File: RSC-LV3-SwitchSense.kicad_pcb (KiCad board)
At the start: 2 copper layers, 140 x 85 mm, 169 parts, among them J1 FTSH-105-01-L-DV-K-A, J10 Molex 43045-0400, J11 Molex 43045-0400, J12 Molex 43045-0400, J13 Molex 43045-0400, J14 Molex 43045-0400, J15 Molex 43045-0400, J16 Molex 43650-0200, J2 USB_C_Receptacle_USB2.0_16P, J3 Molex 43650-0500, J4 Molex 43650-0500, J5 Molex 43650-0200, J6 Molex 43045-0400, J7 Molex 43045-0400, J8 Molex 43045-0400, J9 Molex 43045-0400, Q1 AO3400A, Q10 AO3400A, Q2 AO3400A, Q3 AO3400A, Q4 AO3400A, Q5 AO3400A, Q6 AO3400A, Q7 AO3400A, Q8 AO3400A, Q9 AO3400A, U1 STM32G0B1CBTx, U2 TPS54302, U3 TLV74033PDBVR, U4 TJA1051T-3, U5 TJA1051T-3, Y1 Crystal_GND24, Y2 32.768 kHz 6pF

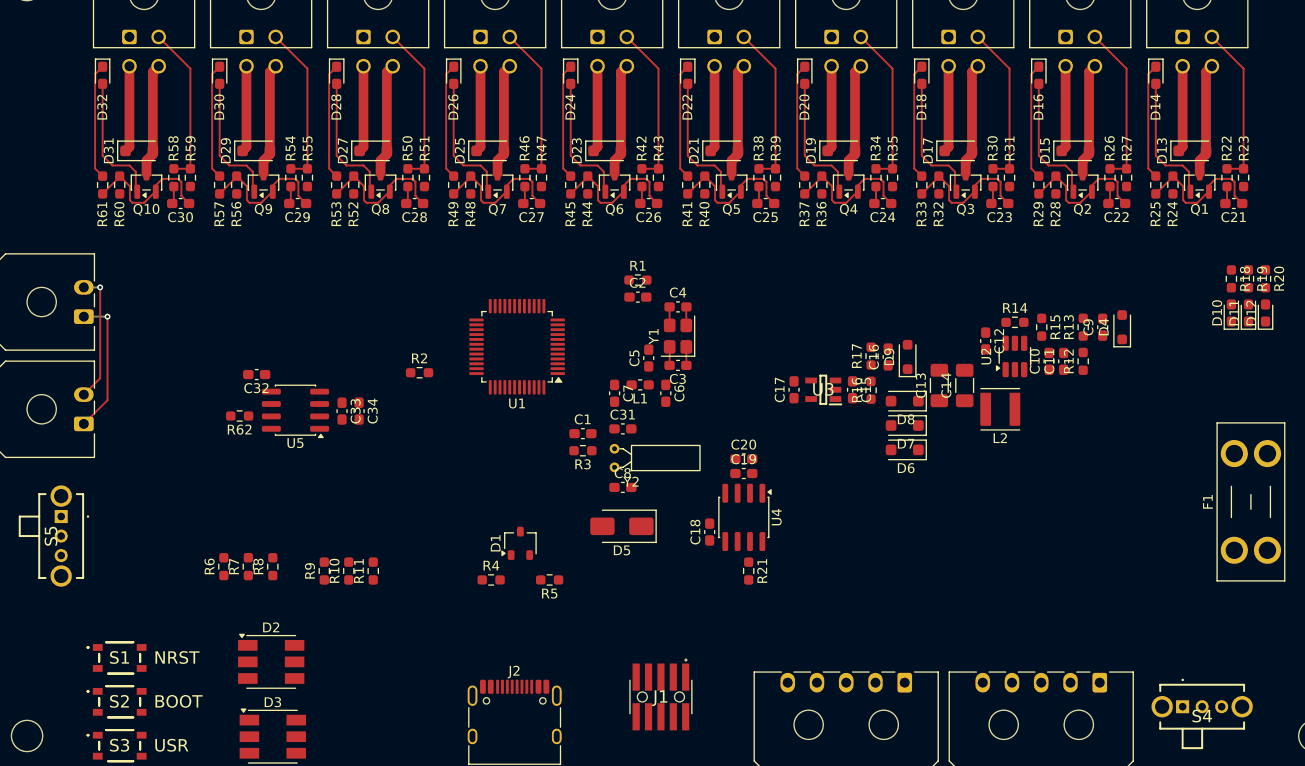
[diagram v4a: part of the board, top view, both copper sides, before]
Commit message: dual H/V compatible Molex footprints, corrected STM32 pinout
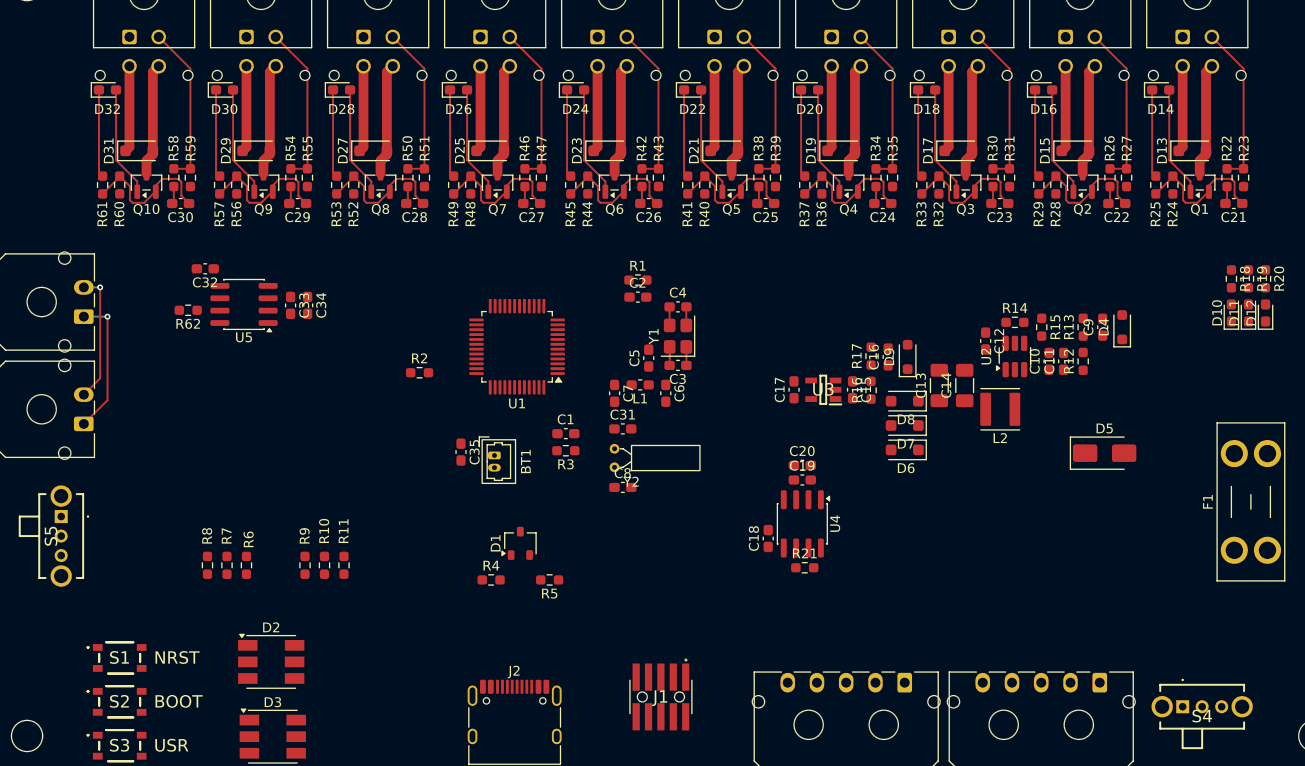
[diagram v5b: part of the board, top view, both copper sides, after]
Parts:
- added BT1: Molex 53047-0210, Connector_Molex:Molex_PicoBlade_53047-0210_1x02_P1.25mm_Vertical, F.Cu at (121.9, 102.2)
- added C35: 1u, Capacitor_SMD:C_0603_1608Metric_Pad1.08x0.95mm_HandSolder, F.Cu at (118.5, 101.9)
- J10, J11, J12, J13, J14, J15, J6, J7, J8, J9: footprint Connector_Molex:Molex_Micro-Fit_3.0_43045-0400_2x02_P3.00mm_Horizontal -> Project_Library:Molex_Micro-Fit_3.0_43045-0400_2x02_P3.00mm_Horizontal_VerticalCompatible
- J16, J5: footprint Connector_Molex:Molex_Micro-Fit_3.0_43650-0200_1x02_P3.00mm_Horizontal -> Project_Library:Molex_Micro-Fit_3.0_43650-0200_1x02_P3.00mm_Horizontal_VerticalCompatible
- J3, J4: footprint Connector_Molex:Molex_Micro-Fit_3.0_43650-0500_1x05_P3.00mm_Horizontal -> Project_Library:Molex_Micro-Fit_3.0_43650-0500_1x05_P3.00mm_Horizontal_VerticalCompatible
- moved D5 50.1 mm to (184.5, 102.0), turned to 0 degrees
- moved U5 12.1 mm to (96.2, 86.8)
- moved C32 12.1 mm to (92.3, 83.1)
- moved C33 12.1 mm to (101.0, 86.8)
- moved C34 12.1 mm to (102.8, 86.8)
- moved R62 12.1 mm to (90.5, 87.3)
- moved R8 6.70 mm to (92.5, 113.5), turned to -90 degrees
- moved C18 6.04 mm to (150.0, 110.8)
- moved C19 6.04 mm to (153.5, 104.8)
- moved C20 6.04 mm to (153.5, 103.2)
- moved U4 6.04 mm to (153.5, 109.2)
- moved R21 5.76 mm to (153.8, 113.8), turned to 0 degrees
- moved R11 3.06 mm to (106.5, 113.5)
- moved R10 2.56 mm to (104.5, 113.5)
- moved R6 2.32 mm to (96.5, 113.5), turned to -90 degrees
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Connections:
- J1 pad 2: BOOT0 -> SWD_IO
- J1 pad 4: SWD_CLK -> BOOT0
- U1 pad 25: unconnected-(U1-PB13-Pad25) -> FDCAN2_TX
- U1 pad 31: unconnected-(U1-PC7-Pad31) -> OUT_2
- U1 pad 35: SWD_CLK -> SWD_IO
- U1 pad 38: FDCAN1_TX -> FDCAN1_RX
- U1 pad 39: FDCAN1_RX -> FDCAN1_TX
- U1 pad 4: unconnected-(U1-VBAT-Pad4) -> Net-(BT1-+)
- U1 pad 44: OUT_2 -> FDCAN2_RX
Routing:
- net Net-(D32-K): track 11.9 -> 8.92 mm
- net Net-(D30-K): track 11.9 -> 8.92 mm
- net Net-(D26-K): track 11.9 -> 8.92 mm
- net Net-(D22-K): track 11.9 -> 8.92 mm
- net Net-(D20-K): track 11.9 -> 8.92 mm
- net Net-(D16-K): track 11.9 -> 8.92 mm
- net Net-(D28-K): track 11.9 -> 8.92 mm
- net Net-(D24-K): track 11.9 -> 8.92 mm
- net Net-(D18-K): track 11.9 -> 8.92 mm
- net Net-(D14-K): track 11.9 -> 8.92 mm
- net OUT_7: track 13.6 -> 11.2 mm
- net OUT_6: track 13.6 -> 11.2 mm
- net OUT_5: track 13.6 -> 11.2 mm
- net OUT_4: track 13.6 -> 11.2 mm
- net OUT_3: track 13.6 -> 11.2 mm
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
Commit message: initial routing
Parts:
- moved R1 54.2 mm to (91.0, 113.5), turned to 90 degrees
- moved C2 51.6 mm to (93.0, 113.5), turned to 90 degrees
- moved R21 35.3 mm to (189.0, 115.0)
- moved C1 34.0 mm to (98.0, 113.5), turned to 90 degrees
- moved R3 31.5 mm to (100.0, 113.5), turned to -90 degrees
- moved R2 27.2 mm to (95.5, 113.5), turned to -90 degrees
- moved BT1 23.0 mm to (144.8, 105.0)
- moved C35 19.9 mm to (138.0, 98.0)
- moved R62 14.2 mm to (90.2, 101.5), turned to -90 degrees
- moved R8 14.0 mm to (106.5, 113.5)
- moved R18 12.4 mm to (205.2, 93.8), turned to 90 degrees
- moved R20 10.2 mm to (197.8, 93.8), turned to 90 degrees
- moved R7 10.0 mm to (104.5, 113.5)
- moved R19 9.88 mm to (201.5, 93.8), turned to 90 degrees
- moved D10 7.97 mm to (205.2, 89.5), turned to -90 degrees
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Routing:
- net +5V_USB: track 0.00 -> 78.9 mm
- net PRIMARY_CAN-: track 0.00 -> 59.7 mm, vias 0 -> 2
- net +12V_IN: track 0.00 -> 59.7 mm
- net +5V_BUS: track 0.00 -> 57.8 mm, vias 0 -> 2
- net PRIMARY_CAN+: track 0.00 -> 57.4 mm, vias 0 -> 3
- net BTN_USR1: track 0.00 -> 30.3 mm
- net +3.3V: track 0.00 -> 29.8 mm
- net AUX_CAN+: track 13.4 -> 39.6 mm, vias 1 -> 3
- net AUX_CAN-: track 14.4 -> 38.8 mm
- net Net-(D3-RK): track 0.00 -> 23.4 mm
- net +5V: track 0.00 -> 23.0 mm
- net BOOT0: track 0.00 -> 22.7 mm
- net +5V_BUCK: track 0.00 -> 21.3 mm, vias 0 -> 2
- net Net-(D3-GK): track 0.00 -> 20.8 mm
- net Net-(S5-NO): track 0.00 -> 19.9 mm
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
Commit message: more non-autorouting adjustments
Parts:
- moved BT1 0.75 mm to (144.8, 105.8)
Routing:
- net USB-: track 14.3 -> 37.1 mm
- net USB+: track 14.3 -> 36.4 mm
- net GND: track 165.8 -> 167.5 mm, vias 0 -> 1
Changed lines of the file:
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@@
 	(footprint "Connector_Molex:Molex_PicoBlade_53047-0210_1x02_P1.25mm_Vertical"
 		(layer "F.Cu")
-		(at 144.75 105 -90)
+		(at 144.75 105.75 -90)
 		(descr "Molex PicoBlade Connector System, 53047-0210, 2 Pins per row (http://www.molex.com/pdm_docs/sd/530470610_sd.pdf)")
 		(tags "connector Molex PicoBlade vertical")
@@
 	)
 	(segment
+		(start 124.5 112.3)
+		(end 124.5 114)
+		(width 0.2)
+		(layer "F.Cu")
+		(net "GND")
+	)
+	(segment
 		(start 168.55 74.6375)
 		(end 168.55 76.065552)
@@
 		(net "GND")
 	)
+	(via
+		(at 124.5 114)
+		(size 0.6)
+		(drill 0.3)
+		(layers "F.Cu" "B.Cu")
+		(net "GND")
+	)
 	(segment
 		(start 81.375 73.2125)
@@
 	)
 	(segment
-		(start 137 99.166722)
-		(end 137 98.1375)
+		(start 143.583278 105.75)
+		(end 137 99.166722)
 		(width 0.2)
 		(layer "F.Cu")
@@
 	)
 	(segment
-		(start 142.833278 105)
-		(end 137 99.166722)
+		(start 137 98.1375)
+		(end 138 97.1375)
 		(width 0.2)
 		(layer "F.Cu")
@@
 	)
 	(segment
-		(start 144.75 105)
-		(end 142.833278 105)
+		(start 137 99.166722)
+		(end 137 98.1375)
 		(width 0.2)
 		(layer "F.Cu")
@@
 	)
 	(segment
-		(start 137 98.1375)
-		(end 138 97.1375)
+		(start 144.75 105.75)
+		(end 143.583278 105.75)
 		(width 0.2)
 		(layer "F.Cu")
@@
 	)
 	(segment
+		(start 125.15 113.649999)
+		(end 125.45 113.949999)
+		(width 0.2)
+		(layer "F.Cu")
+		(net "USB+")
+	)
+	(segment
+		(start 122.475 97.593198)
+		(end 122.475 106.906802)
+		(width 0.2)
+		(layer "F.Cu")
+		(net "USB+")
+	)
+	(segment
 		(start 124.75 124.867499)
 		(end 124.725 124.842499)
@@
 	)
 	(segment
+		(start 124.706249 96.725)
+		(end 123.343198 96.725)
+		(width 0.2)
+		(layer "F.Cu")
+		(net "USB+")
+	)
+	(segment
+		(start 122.475 106.906802)
+		(end 124.725 109.156802)
+		(width 0.2)
+		(layer "F.Cu")
+		(net "USB+")
+	)
+	(segment
 		(start 124.75 126.71241)
 		(end 124.75 125.955)
@@
 	)
 	(segment
+		(start 125.8375 96.75)
+		(end 124.731249 96.75)
+		(width 0.2)
+		(layer "F.Cu")
+		(net "USB+")
+	)
+	(segment
 		(start 124.48241 126.98)
 		(end 124.75 126.71241)
@@
 	)
 	(segment
+		(start 123.343198 96.725)
+		(end 122.475 97.593198)
+		(width 0.2)
+		(layer "F.Cu")
+		(net "USB+")
+	)
+	(segment
 		(start 124.01759 126.98)
 		(end 124.48241 126.98)
@@
 	)
 	(segment
+		(start 125.15 111.773398)
+		(end 125.15 113.649999)
+		(width 0.2)
+		(layer "F.Cu")
+		(net "USB+")
+	)
+	(segment
+		(start 124.725 109.156802)
+		(end 124.725 111.348398)
+		(width 0.2)
+		(layer "F.Cu")
+		(net "USB+")
+	)
+	(segment
+		(start 124.731249 96.75)
+		(end 124.706249 96.725)
+		(width 0.2)
+		(layer "F.Cu")
+		(net "USB+")
+	)
+	(segment
 		(start 124.725 116.175001)
 		(end 125.45 115.450001)
@@
 	)
 	(segment
+		(start 124.725 111.348398)
+		(end 125.15 111.773398)
+		(width 0.2)
+		(layer "F.Cu")
+		(net "USB+")
+	)
+	(segment
+		(start 125.45 113.949999)
+		(end 125.45 114.7)
+		(width 0.2)
+		(layer "F.Cu")
+		(net "USB+")
+	)
+	(segment
 		(start 123.55 115.450001)
 		(end 123.55 114.7)
@@
 	)
 	(segment
+		(start 122.025 97.406802)
+		(end 122.025 107.093198)
+		(width 0.2)
+		(layer "F.Cu")
+		(net "USB-")
+	)
+	(segment
 		(start 124.25 124.867499)
 		(end 124.275 124.842499)
@@
 	)
 	(segment
+		(start 124.275 109.343198)
+		(end 124.275 111.348398)
+		(width 0.2)
+		(layer "F.Cu")
+		(net "USB-")
+	)
+	(segment
 		(start 123.51759 124.93)
 		(end 123.25 125.19759)
@@
 	)
 	(segment
+		(start 124.275 111.348398)
+		(end 123.85 111.773398)
+		(width 0.2)
+		(layer "F.Cu")
+		(net "USB-")
+	)
+	(segment
+		(start 123.85 113.649999)
+		(end 123.55 113.949999)
+		(width 0.2)
+		(layer "F.Cu")
+		(net "USB-")
+	)
+	(segment
+		(start 123.55 113.949999)
+		(end 123.55 114.7)
+		(width 0.2)
+		(layer "F.Cu")
+		(net "USB-")
+	)
+	(segment
+		(start 125.8375 96.25)
+		(end 124.731249 96.25)
+		(width 0.2)
+		(layer "F.Cu")
+		(net "USB-")
+	)
+	(segment
+		(start 124.706249 96.275)
+		(end 123.156802 96.275)
+		(width 0.2)
+		(layer "F.Cu")
+		(net "USB-")
+	)
+	(segment
 		(start 124.275 116.175001)
 		(end 123.55 115.450001)
@@
 	)
 	(segment
+		(start 123.85 111.773398)
+		(end 123.85 113.649999)
+		(width 0.2)
+		(layer "F.Cu")
+		(net "USB-")
+	)
+	(segment
+		(start 123.156802 96.275)
+		(end 122.025 97.406802)
+		(width 0.2)
+		(layer "F.Cu")
+		(net "USB-")
+	)
+	(segment
+		(start 124.731249 96.25)
+		(end 124.706249 96.275)
+		(width 0.2)
+		(layer "F.Cu")
+		(net "USB-")
+	)
+	(segment
 		(start 123.25 125.19759)
 		(end 123.25 125.955)
 		(width 0.2)
 		(layer "F.Cu")
+		(net "USB-")
+	)
+	(segment
+		(start 122.025 107.093198)
+		(end 124.275 109.343198)
+		(width 0.2)
+		(layer "F.Cu")

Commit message: initial complete route
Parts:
- moved C32 1.75 mm to (94.0, 83.2), turned to 0 degrees
- turned R24 to -90 degrees
- turned R28 to -90 degrees
- turned R32 to -90 degrees
- turned R36 to -90 degrees
- turned R40 to -90 degrees
- turned R44 to -90 degrees
- turned R48 to -90 degrees
- turned R52 to -90 degrees
- turned R56 to -90 degrees
- turned R60 to -90 degrees
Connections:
- J2 pad SH: (no net) -> GND
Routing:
- net GND: track 167.5 -> 1127.5 mm, vias 1 -> 8
- net +3.3V: track 29.8 -> 355.7 mm, vias 0 -> 17
- net +12V: track 103.5 -> 341.3 mm
- net +5V: track 23.0 -> 143.9 mm, vias 0 -> 4
- net NRST: track 16.2 -> 123.2 mm, vias 0 -> 3
- net BOOT0: track 22.7 -> 107.3 mm, vias 0 -> 2
- net OUT_1: track 11.2 -> 93.0 mm, vias 0 -> 2
- net IN_1: track 1.80 -> 72.0 mm, vias 0 -> 2
- net OUT_2: track 11.2 -> 76.2 mm
- net V_SENSE_12: track 5.66 -> 68.0 mm, vias 0 -> 2
- net IN_2: track 1.80 -> 61.5 mm, vias 0 -> 2
- net STAT1_G: track 0.00 -> 55.3 mm, vias 0 -> 2
- net STAT0_G: track 0.00 -> 53.3 mm
- net STAT1_B: track 0.00 -> 52.2 mm
- net OUT_10: track 11.2 -> 60.7 mm, vias 0 -> 2
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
